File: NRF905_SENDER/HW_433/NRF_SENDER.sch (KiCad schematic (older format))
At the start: 21 parts, among them J1 SWD, SW1 SW_Push, SW2 SW_Push, U1 STM32L031F6Px

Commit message: Change MCU. New MCU STM32L051
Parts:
- removed R2, R3, R4, R7, R8, R9: 10 k, Resistor_SMD:R_0603_1608Metric_Pad1.05x0.95mm_HandSolder, symbol Device:R
- removed R5: 120, Resistor_SMD:R_0603_1608Metric_Pad1.05x0.95mm_HandSolder, symbol Device:R
- removed U1: STM32L031F6Px, Package_SO:TSSOP-20_4.4x6.5mm_P0.65mm, symbol MCU_ST_STM32L0:STM32L031F6Px
- added U?: STM32L051C6Tx, Package_QFP:LQFP-48_7x7mm_P0.5mm, symbol MCU_ST_STM32L0:STM32L051C6Tx
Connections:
- wire segments 148 -> 90
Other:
- moved on the sheet: J1

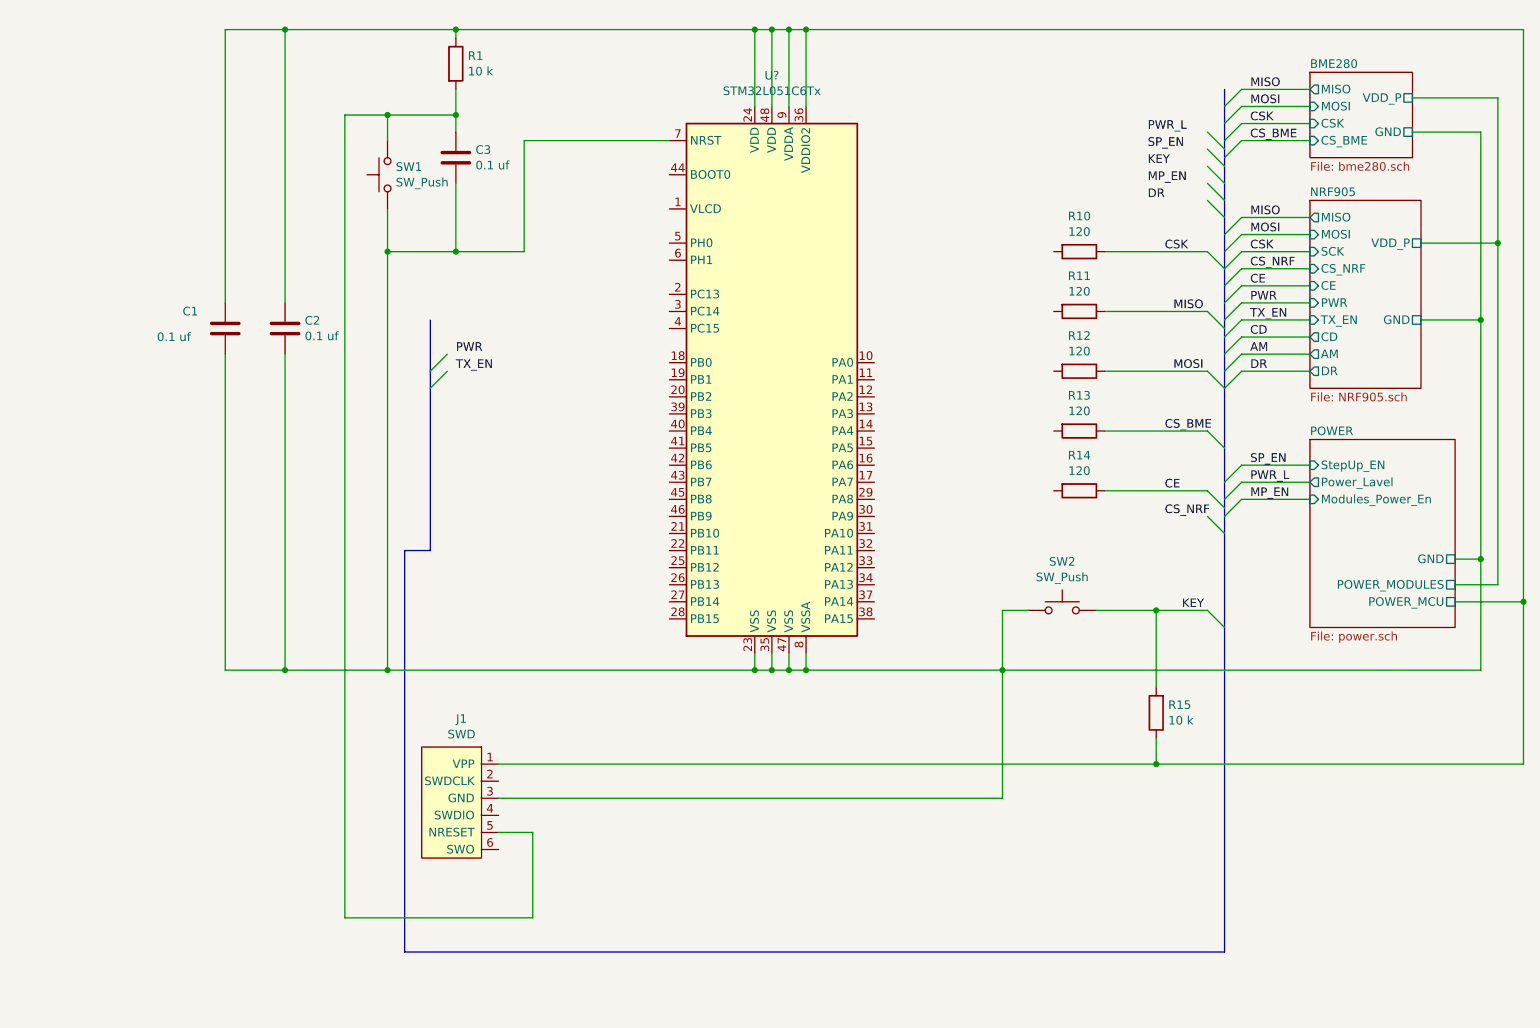
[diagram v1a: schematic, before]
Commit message: new scematics. New PCB.
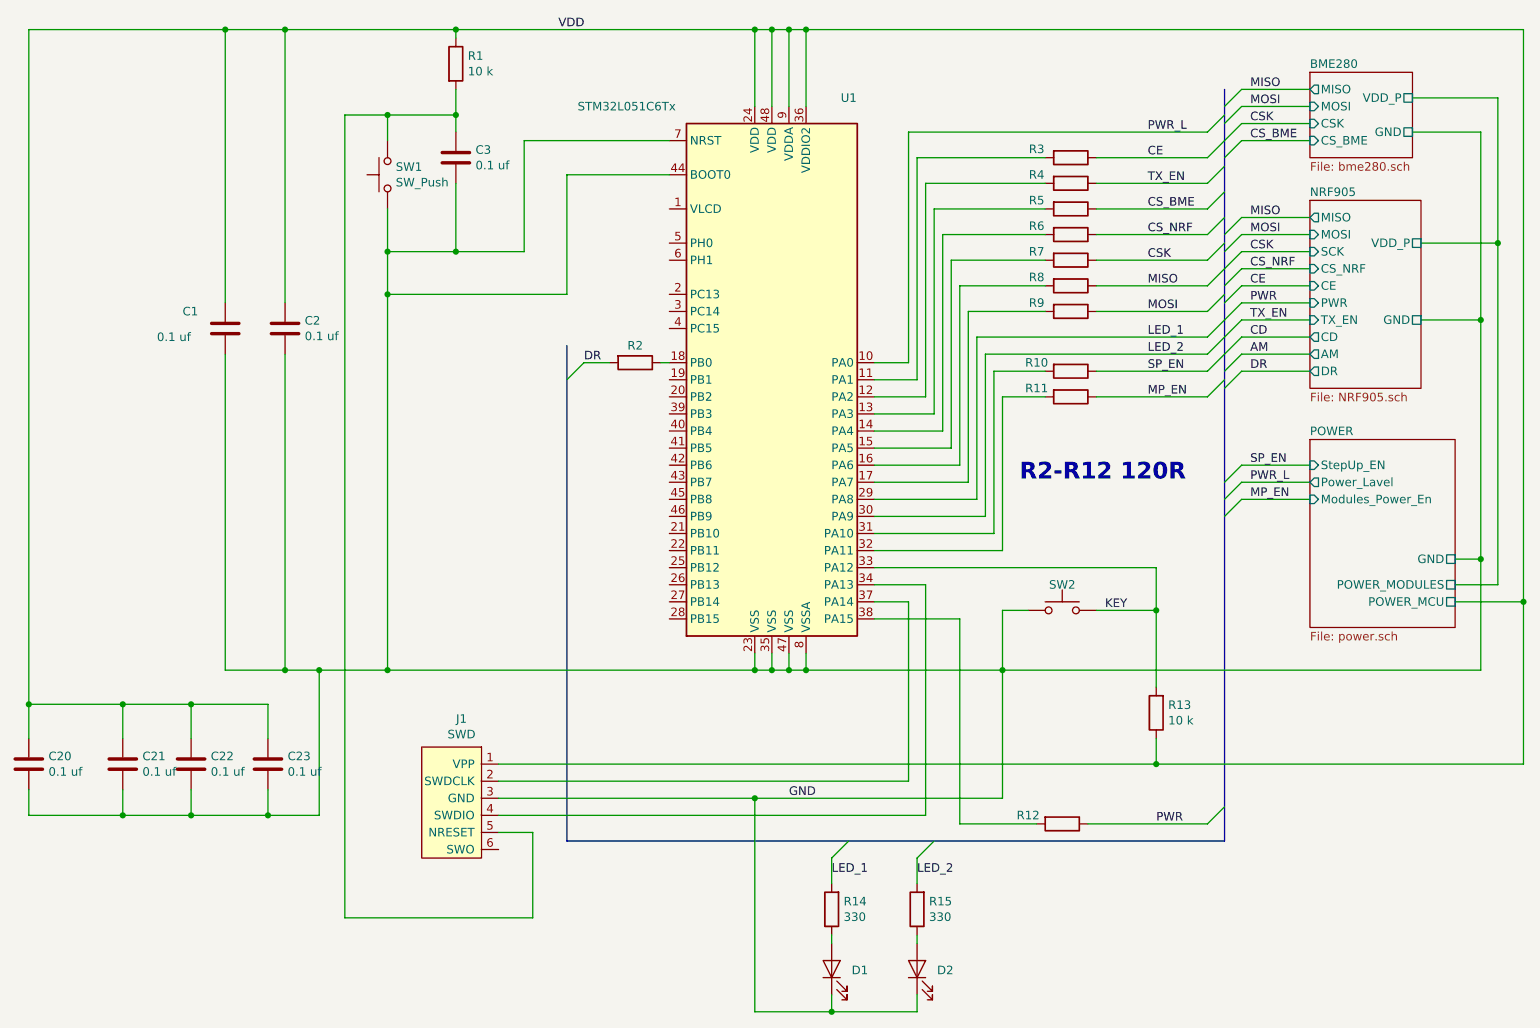
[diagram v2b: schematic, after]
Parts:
- added C20, C21, C22, C23: 0.1 uf, Capacitor_SMD:C_0603_1608Metric_Pad1.05x0.95mm_HandSolder, symbol Device:C
- added D1, D2: LED, LED_SMD:LED_0603_1608Metric_Pad1.05x0.95mm_HandSolder, symbol Device:LED
- added R10, R11, R12, R2, R8, R9: 120, Resistor_SMD:R_0603_1608Metric_Pad1.05x0.95mm_HandSolder, symbol Device:R
- added R14, R15: 330, Resistor_SMD:R_0603_1608Metric_Pad1.05x0.95mm_HandSolder, symbol Device:R
- gave numbers to parts that had none: 1
- renumbered R15 to R13, R10 to R3, R11 to R4, R12 to R5, R13 to R6, R14 to R7
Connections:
- net BME280/GND is gone; now on net GND: C1.2, C2.2, C3.2, J1.3 (GND), SW1.1, SW2.1, U1.23 (VSS), U1.35 (VSS), U1.47 (VSS), U1.7 (NRST), U1.8 (VSSA)
- net CE: now also R3.1; no longer R7.1
- net CSK: now also R7.1; no longer R3.1
- net CS_BME: now also R5.1; no longer R6.1
- net CS_NRF: now also R6.1
- net DR: now also R2.2
- net KEY: now also U1.33 (PA12)
- net MISO: now also R8.1; no longer R4.1
- net MOSI: now also R9.1; no longer R5.1
- net MP_EN: now also R11.1
- net PWR: now also R12.1
- net PWR_L: now also U1.10 (PA0)
- net SP_EN: now also R10.1
- net TX_EN: now also R4.1
- net at R3.2: now also U1.11 (PA1)
- net at R4.2: now also U1.12 (PA2)
- net at R5.2: now also U1.13 (PA3)
- net at R6.2: now also U1.14 (PA4)
- net at R7.2: now also U1.15 (PA5)
- net at J1.2 (SWDCLK): now also U1.37 (PA14)
- net at J1.4 (SWDIO): now also U1.34 (PA13)
- net at U1.16 (PA6): now also R8.2
- net at U1.17 (PA7): now also R9.2
- net at U1.18 (PB0): now also R2.1
- net LED_1: now reaches U1.29 (PA8)
- net LED_1: now also R14.2
- net LED_2: now reaches U1.30 (PA9)
- net LED_2: now also R15.2
- net at U1.31 (PA10): now also R10.2
- net at U1.32 (PA11): now also R11.2
- net at U1.38 (PA15): now also R12.2
- net GND: now reaches U1.44 (BOOT0)
- net GND: now also C20.2, C21.2, C22.2, C23.2, D1.1 (K), D2.1 (K)
- net POWER/POWER_MCU renamed VDD
- net VDD: now also C20.1, C21.1, C22.1, C23.1
- new net: D2.2 (A), R15.1
- new net: D1.2 (A), R14.1
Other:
- note added: "R2-R12 120R"
- moved on the sheet: R3, R4, R5, R6, R7
